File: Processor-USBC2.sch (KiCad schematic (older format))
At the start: 46 parts, among them J14 Conn_02x05_Odd_Even, J15 201267-0005, Q11 AOSD21307, Q12 AOSD21307, U23 HD3SS460RHRR, U24 CYPD5125-40LQXIT, U25 PESD5V0X1BQ,115, U26 DF10G5M4N,LF, U27 DF10G5M4N,LF

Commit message: PVT
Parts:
- removed C86: 100n, Capacitor-Chip:C_CHIP_1005_Hand_NoSilk, symbol passive:C
- removed R67, R69: 10k, Resistor-Chip:R_CHIP_1005_Hand_NoSilk, symbol passive:R
- removed TP28: TX, Print:TP_C0.8, symbol print:TestPoint
- removed TP29: RX, Print:TP_C0.8, symbol print:TestPoint
- removed U26, U27: DF10G5M4N,LF, IC-SON:USON10_2.5x1.0_P0.5, symbol interface-ti:TPD4E02B04
- added Q11: BSS138W, IC-SOP:SC70-3, symbol transistor-mos:Q_NMOS_GSD
- added RA1: 4.7k, Resistor-Chip:R_CHIP_4x1005_CONCAVE, symbol passive:R_Array_4
- added U24, U25: DF10G5M4N,LF, IC-SON:USON10_2.5x1.0_P0.5, symbol interface-ti:TPD4E02B04
- C81: renamed from C83; PartName C1005X5R1V105K050BE -> TMK105BJ105MV-F
- C82: renamed from C87; PartName C1005X5R1V105K050BE -> TMK105BJ105MV-F
- C92: renamed from C97; PartName C1005X5R1V105K050BE -> TMK105BJ105MV-F
- C96: renamed from C101; PartName UMK325BJ106MM-P -> GMK325BJ106KN-T
- R62: renamed from R71; value 10m -> 20m; PartName ERJ-8CWJR010V -> ERJ-8CWJR020V
- R67: renamed from R76; footprint Resistor-Chip:R_CHIP_1608_Reflow -> Resistor-Chip:R_CHIP_1005_Hand_NoSilk; PartName RK73Z1JTTD -> RK73Z1ETTP
- renumbered C80 to C76, C81 to C77, C82 to C78, C84 to C79, C85 to C80, C88 to C83, C89 to C84, C90 to C85, C91 to C86, C92 to C87, C93 to C88, C94 to C89, C95 to C90, C96 to C91, C98 to C93, C99 to C94, C100 to C95, C102 to C97, C103 to C98, Q11 to Q12, Q12 to Q13, R70 to R60, R68 to R61, R72 to R63, R73 to R64, R75 to R65, R74 to R66, TP30 to TP28, U23 to U21, U24 to U22, U25 to U23
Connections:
- net CRX1+: now also U24.5 (IO4), U24.6 (NC)
- net CRX1-: now also U24.4 (IO3), U24.7 (NC)
- net CRX2+: now also U25.4 (IO3), U25.7 (NC)
- net CRX2-: now also U25.5 (IO4), U25.6 (NC)
- net CTX1_AC+: now also U24.2 (IO2), U24.9 (NC)
- net CTX1_AC-: now also U24.1 (IO1), U24.10 (NC)
- net CTX2_AC+: now also U25.1 (IO1), U25.10 (NC)
- net CTX2_AC-: now also U25.2 (IO2), U25.9 (NC)
- net DP_HPD: now also Q11.2 (S), RA1.D1
- net GND: now also RA1.D2, U24.3 (GND), U24.8 (GND), U25.3 (GND), U25.8 (GND)
- net HPD: now also Q11.1 (G)
- net SNK_S: now also Q12.3 (S), Q13.1 (S), R66.1; no longer Q12.1 (S), Q13.3 (S), R65.1
- net SRC_S: now also Q12.1 (S), Q13.3 (S), R65.1; no longer Q12.3 (S), Q13.1 (S), R66.1
- net USB5V: now also Q12.7 (D), Q12.8 (D); no longer Q12.5 (D), Q12.6 (D)
- net USBSS_TX+: now also U21.26 (SSTXp); no longer U21.25 (SSTXn)
- net USBSS_TX-: now also U21.25 (SSTXn); no longer U21.26 (SSTXp)
- net VBUS: now also Q12.5 (D), Q12.6 (D); no longer Q12.7 (D), Q12.8 (D)
- net VDDD: now also C83.1, U21.22 (VCC)
- net at Q12.4 (G), Q13.2 (G), R66.2: now also U22.12 (VBUS_C_CTRL); no longer U22.11 (VBUS_P_CTRL)
- net at Q12.2 (G), Q13.4 (G), R65.2: now also U22.11 (VBUS_P_CTRL); no longer U22.12 (VBUS_C_CTRL)
- removed net MUX_VCC: C83.1, U21.22 (VCC), U22.15 (P2.2/I2C_INT_EC)
- new net +1V8: Q11.3 (D)
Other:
- moved on the sheet: C81, Q12A, Q12B, Q13A, Q13B, R61, R65, R66, TP28

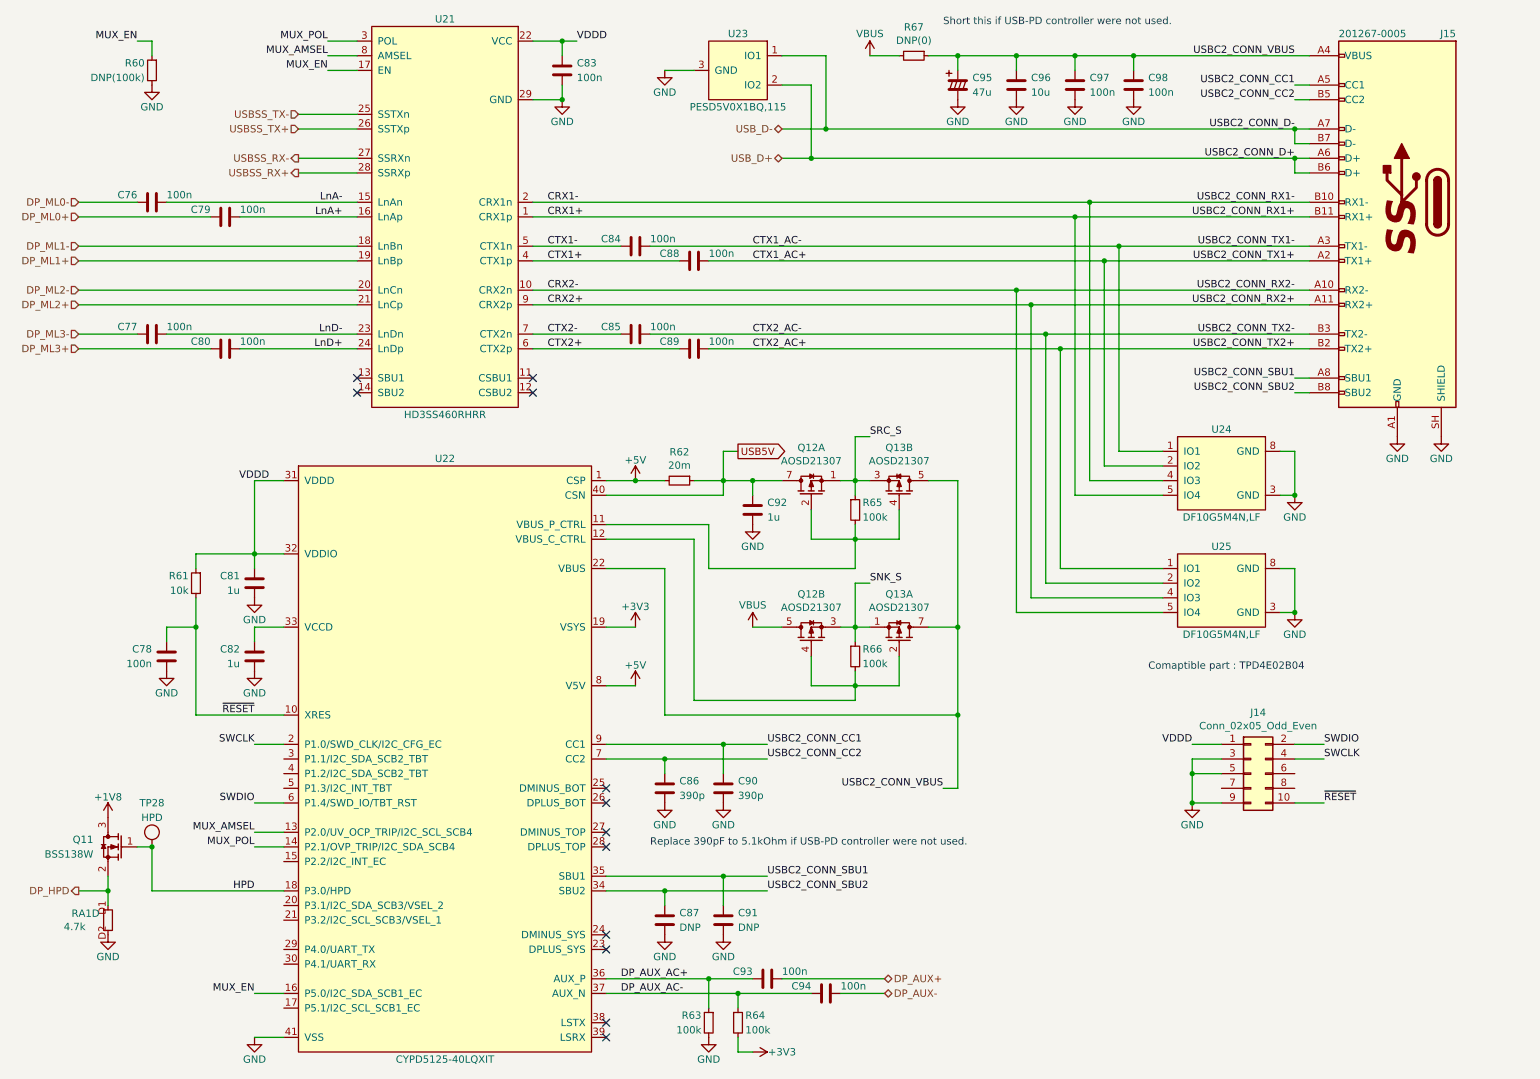
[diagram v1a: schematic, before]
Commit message: SBUにTVSダイオードを追加
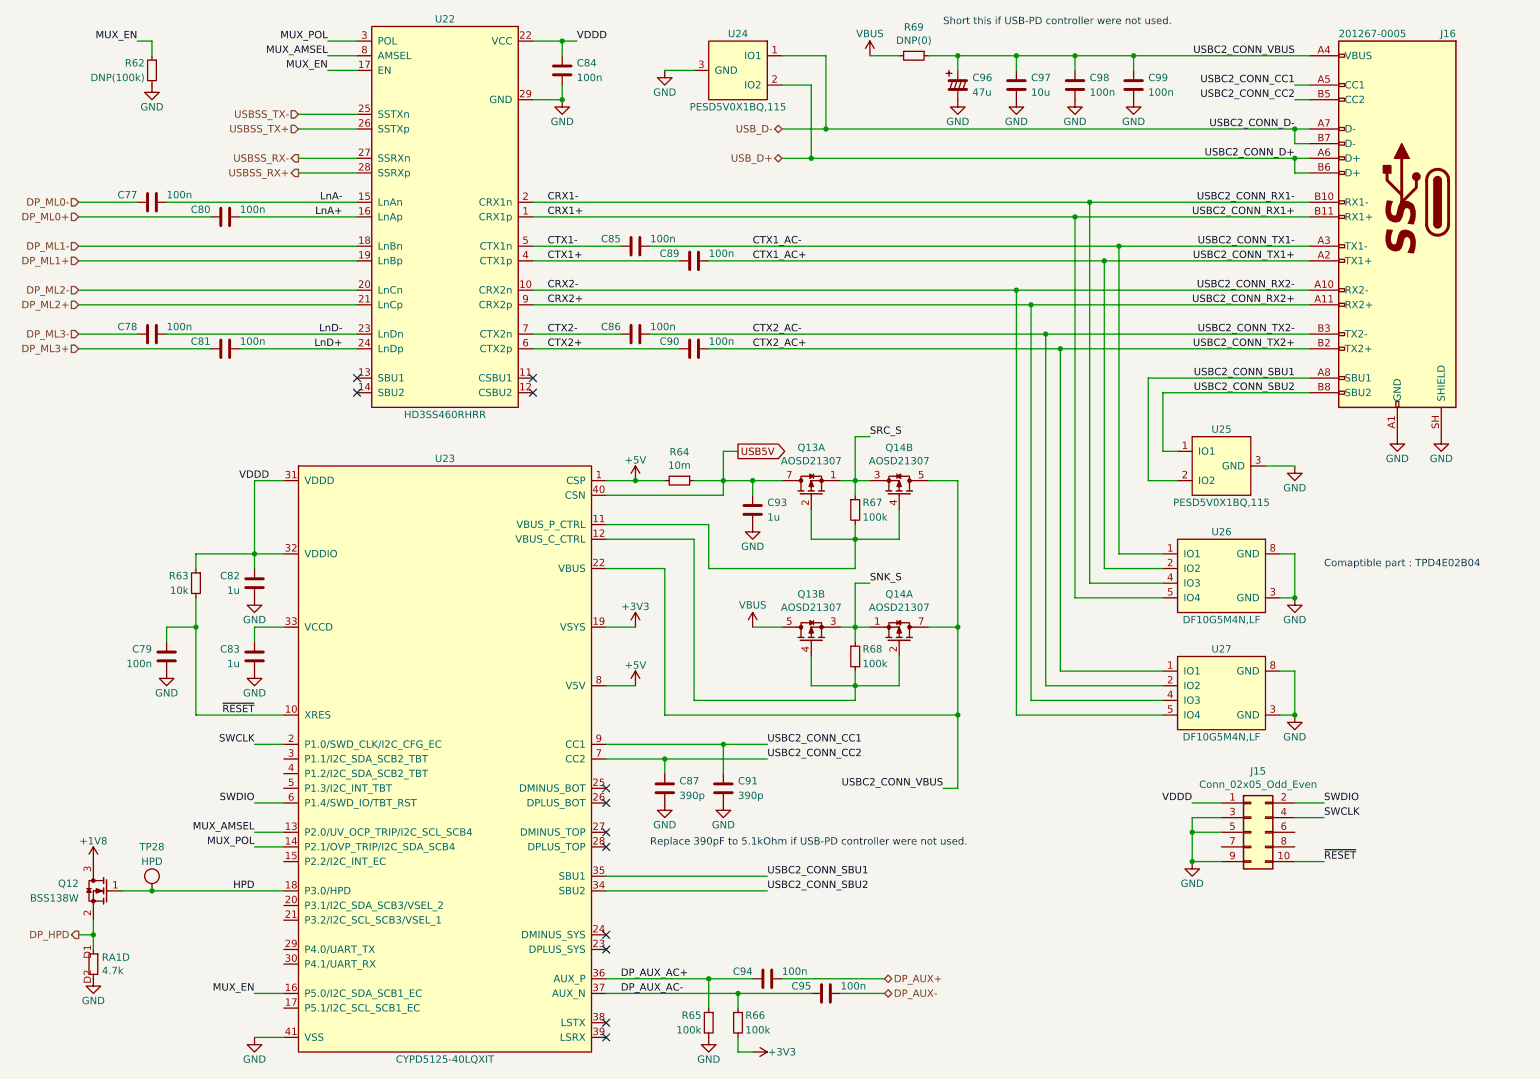
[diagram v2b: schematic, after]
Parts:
- removed C87, C91: DNP, Capacitor-Chip:C_CHIP_1005_Hand_NoSilk, symbol passive:C
- removed Q11: BSS138W, IC-SOP:SC70-3, symbol transistor-mos:Q_NMOS_GSD
- added Q12: BSS138W, IC-SOP:SC70-3, symbol transistor-mos:Q_NMOS_GSD
- added U25: PESD5V0X1BQ,115, IC-SOT:SOT663, symbol protection:TVS_2CH_1_2_GND3
- R64: renamed from R62; value 20m -> 10m; PartName ERJ-8CWJR020V -> ERJ-8CWJR010V
- U24: renamed from U23; value PESD5V0X1BQ,115 -> PESD5V0X1BQ,115
- renumbered C76 to C77, C77 to C78, C78 to C79, C79 to C80, C80 to C81, C81 to C82, C82 to C83, C83 to C84, C84 to C85, C85 to C86, C86 to C87, C88 to C89, C89 to C90, C90 to C91, C92 to C93, C93 to C94, C94 to C95, C95 to C96, C96 to C97, C97 to C98, C98 to C99, J14 to J15, J15 to J16, Q12 to Q13, Q13 to Q14, R60 to R62, R61 to R63, R63 to R65, R64 to R66, R65 to R67, R66 to R68, R67 to R69, U21 to U22, U22 to U23, U24 to U26, U25 to U27
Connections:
- net +1V8: now also Q12.3 (D)
- net DP_HPD: now also Q12.2 (S)
- net GND: now also U25.3 (GND)
- net HPD: now also Q12.1 (G)
- net USBC2_CONN_SBU1: now also U25.2 (IO2)
- net USBC2_CONN_SBU2: now also U25.1 (IO1)
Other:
- moved on the sheet: J15, RA1D, TP28, U26, U27
